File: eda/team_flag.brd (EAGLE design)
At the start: 40.6 x 40.6 mm, 25 parts, among them Q1 IRFML8244, Q2 IRFML8244

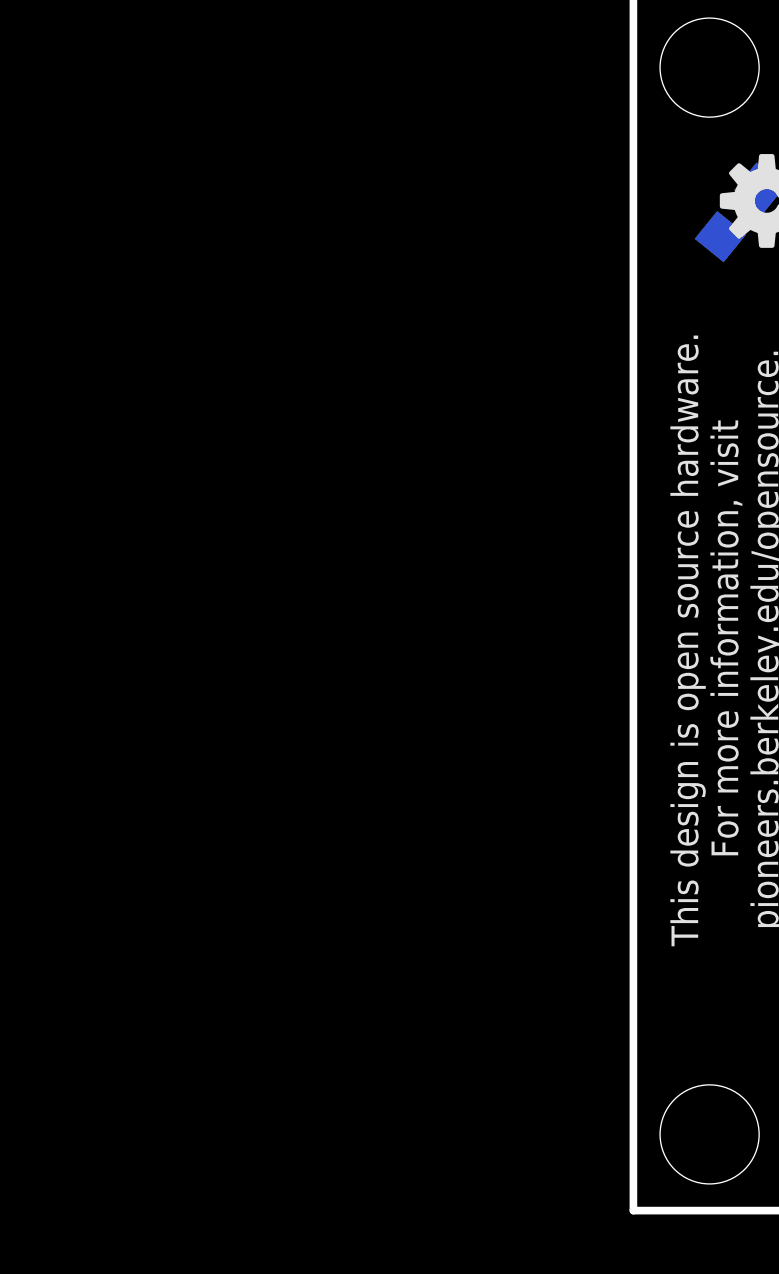
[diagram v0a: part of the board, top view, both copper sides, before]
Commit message: Add Arduino Pro Micro breakout and connect nets on schematic
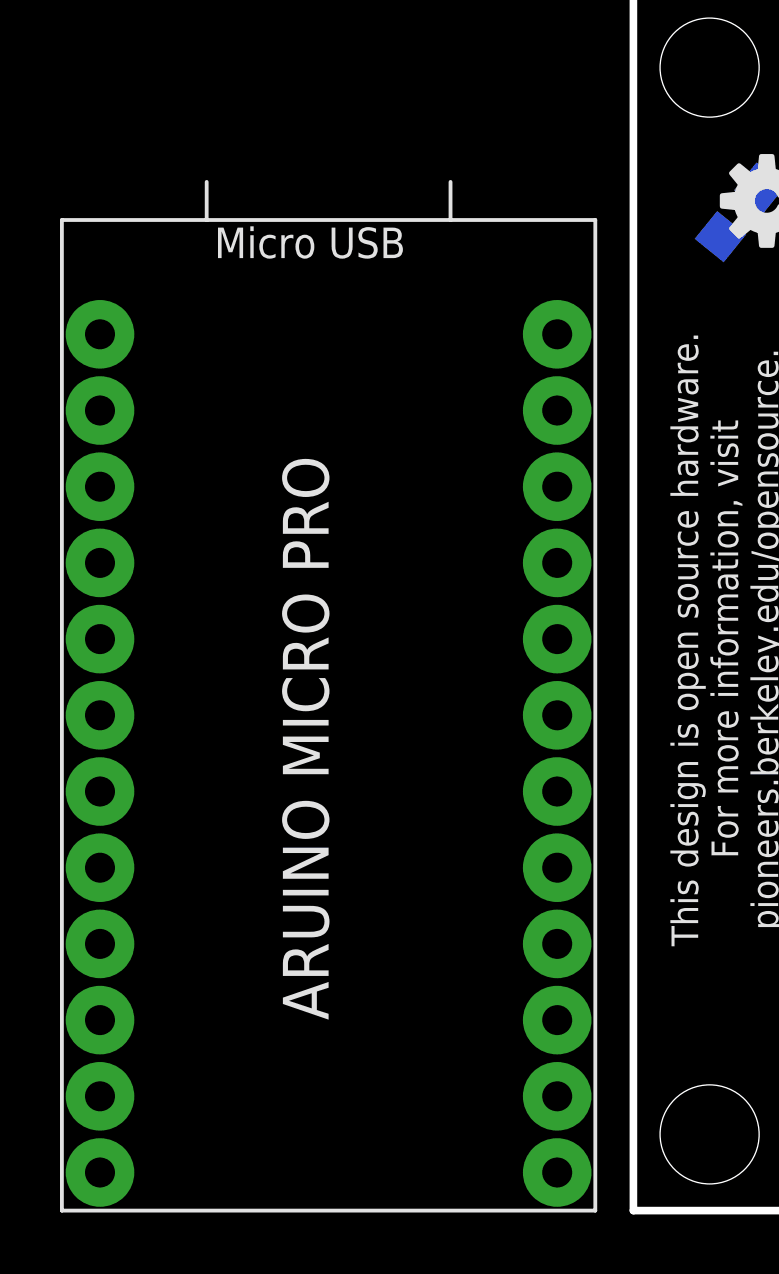
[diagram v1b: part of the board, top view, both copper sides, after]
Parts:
- added U$3: ARDUINO_PRO_MICRO, pie:ARDUINO_PRO_MICRO
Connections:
- net 5V: now also U$3.VCC
- net BLUE(IO1): now also U$3.5
- net GND: now also U$3.GND@0, U$3.GND@1, U$3.GND@2
- net LED1: now also U$3.A3
- net LED2: now also U$3.A2
- net LED3: now also U$3.A1
- net LED4: now also U$3.A0
- net YELLOW(IO2): now also U$3.6
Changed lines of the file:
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@@
 <layer number="54" name="bGND_GNDA" color="1" fill="9" visible="no" active="no"/>
 <layer number="56" name="wert" color="7" fill="1" visible="no" active="no"/>
+<layer number="57" name="tCAD" color="7" fill="1" visible="no" active="no"/>
+<layer number="59" name="tCarbon" color="7" fill="1" visible="no" active="no"/>
+<layer number="60" name="bCarbon" color="7" fill="1" visible="no" active="no"/>
 <layer number="90" name="Modules" color="5" fill="1" visible="no" active="no"/>
 <layer number="91" name="Nets" color="2" fill="1" visible="no" active="no"/>
@@
 <layer number="109" name="fp9" color="7" fill="1" visible="yes" active="yes"/>
 <layer number="110" name="fp0" color="7" fill="1" visible="yes" active="yes"/>
+<layer number="111" name="LPC17xx" color="7" fill="1" visible="yes" active="yes"/>
+<layer number="112" name="tSilk" color="7" fill="1" visible="yes" active="yes"/>
+<layer number="113" name="IDFDebug" color="7" fill="1" visible="yes" active="yes"/>
+<layer number="114" name="Badge_Outline" color="11" fill="1" visible="no" active="no"/>
 <layer number="116" name="Patch_BOT" color="9" fill="4" visible="yes" active="yes"/>
+<layer number="118" name="Rect_Pads" color="7" fill="1" visible="yes" active="yes"/>
 <layer number="121" name="_tsilk" color="7" fill="1" visible="yes" active="yes"/>
 <layer number="122" name="_bsilk" color="7" fill="1" visible="yes" active="yes"/>
@@
 <layer number="124" name="bTestmark" color="7" fill="1" visible="yes" active="yes"/>
 <layer number="125" name="_tNames" color="7" fill="1" visible="yes" active="yes"/>
+<layer number="126" name="_bNames" color="7" fill="1" visible="yes" active="yes"/>
+<layer number="127" name="_tValues" color="7" fill="1" visible="yes" active="yes"/>
+<layer number="128" name="_bValues" color="7" fill="1" visible="yes" active="yes"/>
+<layer number="129" name="Mask" color="7" fill="1" visible="yes" active="yes"/>
 <layer number="131" name="tAdjust" color="7" fill="1" visible="yes" active="yes"/>
 <layer number="132" name="bAdjust" color="7" fill="1" visible="yes" active="yes"/>
 <layer number="144" name="Drill_legend" color="7" fill="1" visible="yes" active="yes"/>
+<layer number="150" name="Notes" color="7" fill="1" visible="yes" active="yes"/>
 <layer number="151" name="HeatSink" color="7" fill="1" visible="yes" active="yes"/>
+<layer number="152" name="_bDocu" color="7" fill="1" visible="yes" active="yes"/>
+<layer number="153" name="FabDoc1" color="7" fill="1" visible="yes" active="yes"/>
+<layer number="154" name="FabDoc2" color="7" fill="1" visible="yes" active="yes"/>
+<layer number="155" name="FabDoc3" color="7" fill="1" visible="yes" active="yes"/>
 <layer number="199" name="Contour" color="7" fill="1" visible="yes" active="yes"/>
 <layer number="200" name="200bmp" color="1" fill="10" visible="yes" active="yes"/>
@@
 <layer number="223" name="223bmp" color="24" fill="1" visible="no" active="no"/>
 <layer number="224" name="224bmp" color="25" fill="1" visible="no" active="no"/>
+<layer number="225" name="225bmp" color="7" fill="1" visible="yes" active="yes"/>
+<layer number="226" name="226bmp" color="7" fill="1" visible="yes" active="yes"/>
+<layer number="227" name="227bmp" color="7" fill="1" visible="yes" active="yes"/>
+<layer number="228" name="228bmp" color="7" fill="1" visible="yes" active="yes"/>
+<layer number="229" name="229bmp" color="7" fill="1" visible="yes" active="yes"/>
+<layer number="230" name="230bmp" color="7" fill="1" visible="yes" active="yes"/>
+<layer number="231" name="231bmp" color="7" fill="1" visible="yes" active="yes"/>
+<layer number="248" name="Housing" color="7" fill="1" visible="yes" active="yes"/>
+<layer number="249" name="Edge" color="7" fill="1" visible="yes" active="yes"/>
 <layer number="250" name="Descript" color="3" fill="1" visible="no" active="no"/>
 <layer number="251" name="SMDround" color="12" fill="11" visible="no" active="no"/>
 <layer number="254" name="cooling" color="7" fill="1" visible="yes" active="yes"/>
+<layer number="255" name="routoute" color="7" fill="1" visible="yes" active="yes"/>
 </layers>
 <board>
@@
 <attribute name="VALUE" x="5.45880625" y="31.758984375" size="0.762" layer="26" font="vector" ratio="15" rot="MR309" align="center"/>
 </element>
+<element name="U$3" library="pie" package="ARDUINO_PRO_MICRO" value="ARDUINO_PRO_MICRO" x="-19.05" y="0"/>
 </elements>
 <signals>
@@
 <wire x1="17.46" y1="13.777" x2="17.78" y2="14.097" width="0.3048" layer="1"/>
 <wire x1="17.78" y1="14.097" x2="19.431" y2="14.097" width="0.3048" layer="1"/>
+<contactref element="U$3" pad="6"/>
+<wire x1="-17.78" y1="8.89" x2="17.46" y2="12.938" width="0" layer="19" extent="1-1"/>
 </signal>
 <signal name="GND">
@@
 <via x="13.97" y="26.67" extent="1-16" drill="0.5"/>
 <via x="15.24" y="27.94" extent="1-16" drill="0.5"/>
+<contactref element="U$3" pad="GND@1"/>
+<contactref element="U$3" pad="GND@0"/>
+<contactref element="U$3" pad="GND@2"/>
+<wire x1="32.46468125" y1="37.739371875" x2="36.428628125" y2="34.08331875" width="0" layer="19" extent="16-16"/>
+<wire x1="15.24" y1="27.94" x2="32.46468125" y2="37.739371875" width="0" layer="19" extent="16-16"/>
+<wire x1="13.97" y1="27.94" x2="15.24" y2="27.94" width="0" layer="19" extent="1-1"/>
+<wire x1="12.7" y1="27.94" x2="13.97" y2="27.94" width="0" layer="19" extent="1-1"/>
+<wire x1="13.97" y1="26.67" x2="13.97" y2="27.94" width="0" layer="19" extent="1-1"/>
+<wire x1="6.55668125" y1="36.555625" x2="13.97" y2="30.48" width="0" layer="19" extent="1-16"/>
+<wire x1="2.900628125" y1="32.464678125" x2="6.55668125" y2="36.555625" width="0" layer="19" extent="16-16"/>
+<wire x1="-2.54" y1="26.67" x2="2.900628125" y2="32.464678125" width="0" layer="19" extent="16-16"/>
+<wire x1="15.24" y1="15.025" x2="13.97" y2="26.67" width="0" layer="19" extent="1-1"/>
+<wire x1="15.56" y1="12.938" x2="15.24" y2="15.025" width="0" layer="19" extent="1-1"/>
+<wire x1="20.64" y1="12.938" x2="15.56" y2="12.938" width="0" layer="19" extent="1-1"/>
+<wire x1="20.3454" y1="16.725" x2="20.64" y2="12.938" width="0" layer="19" extent="1-1"/>
+<wire x1="25.4254" y1="16.725" x2="20.3454" y2="16.725" width="0" layer="19" extent="1-1"/>
+<wire x1="-17.78" y1="24.13" x2="-2.54" y2="26.67" width="0" layer="19" extent="1-1"/>
+<wire x1="-17.78" y1="21.59" x2="-17.78" y2="24.13" width="0" layer="19" extent="1-1"/>
 </signal>
 <signal name="BLUE(IO1)">
@@
 <wire x1="22.54" y1="13.777" x2="22.86" y2="14.097" width="0.3048" layer="1"/>
 <wire x1="22.86" y1="14.097" x2="24.511" y2="14.097" width="0.3048" layer="1"/>
+<contactref element="U$3" pad="5"/>
+<wire x1="-17.78" y1="11.43" x2="21.59" y2="7.62" width="0" layer="19" extent="1-1"/>
 </signal>
 <signal name="BSOURCE">
@@
 <wire x1="26.67" y1="25.4" x2="26.67" y2="21.59" width="0.762" layer="1"/>
 <wire x1="26.67" y1="21.59" x2="25.4" y2="20.32" width="0.762" layer="1"/>
+<contactref element="U$3" pad="VCC"/>
+<wire x1="-2.54" y1="21.59" x2="15.24" y2="20.32" width="0" layer="19" extent="16-16"/>
 </signal>
 <signal name="LED4">
@@
 <wire x1="12.7" y1="25.4" x2="16.51" y2="25.4" width="0.3048" layer="1"/>
 <wire x1="11.43" y1="26.67" x2="12.7" y2="25.4" width="0.3048" layer="1"/>
+<contactref element="U$3" pad="A0"/>
+<wire x1="-2.54" y1="11.43" x2="12.7" y2="25.4" width="0" layer="19" extent="1-1"/>
 </signal>
 <signal name="N$4">
@@
 <wire x1="26.67" y1="30.9" x2="24.55" y2="30.9" width="0.3048" layer="1"/>
 <wire x1="24.55" y1="30.9" x2="24.13" y2="30.48" width="0.3048" layer="1"/>
+<contactref element="U$3" pad="A3"/>
+<wire x1="-2.54" y1="19.05" x2="24.13" y2="30.48" width="0" layer="19" extent="1-1"/>
 </signal>
 <signal name="LED2">
@@
 <contactref element="JP1" pad="P$3"/>
 <wire x1="21.59" y1="30.9" x2="21.59" y2="25.4" width="0.3048" layer="1"/>
+<contactref element="U$3" pad="A2"/>
+<wire x1="-2.54" y1="16.51" x2="21.59" y2="25.4" width="0" layer="19" extent="1-1"/>
 </signal>
 <signal name="LED3">
@@
 <wire x1="16.51" y1="30.9" x2="18.63" y2="30.9" width="0.3048" layer="1"/>
 <wire x1="18.63" y1="30.9" x2="19.05" y2="30.48" width="0.3048" layer="1"/>
+<contactref element="U$3" pad="A1"/>
+<wire x1="-2.54" y1="13.97" x2="16.51" y2="30.9" width="0" layer="19" extent="1-1"/>
 </signal>
 </signals>

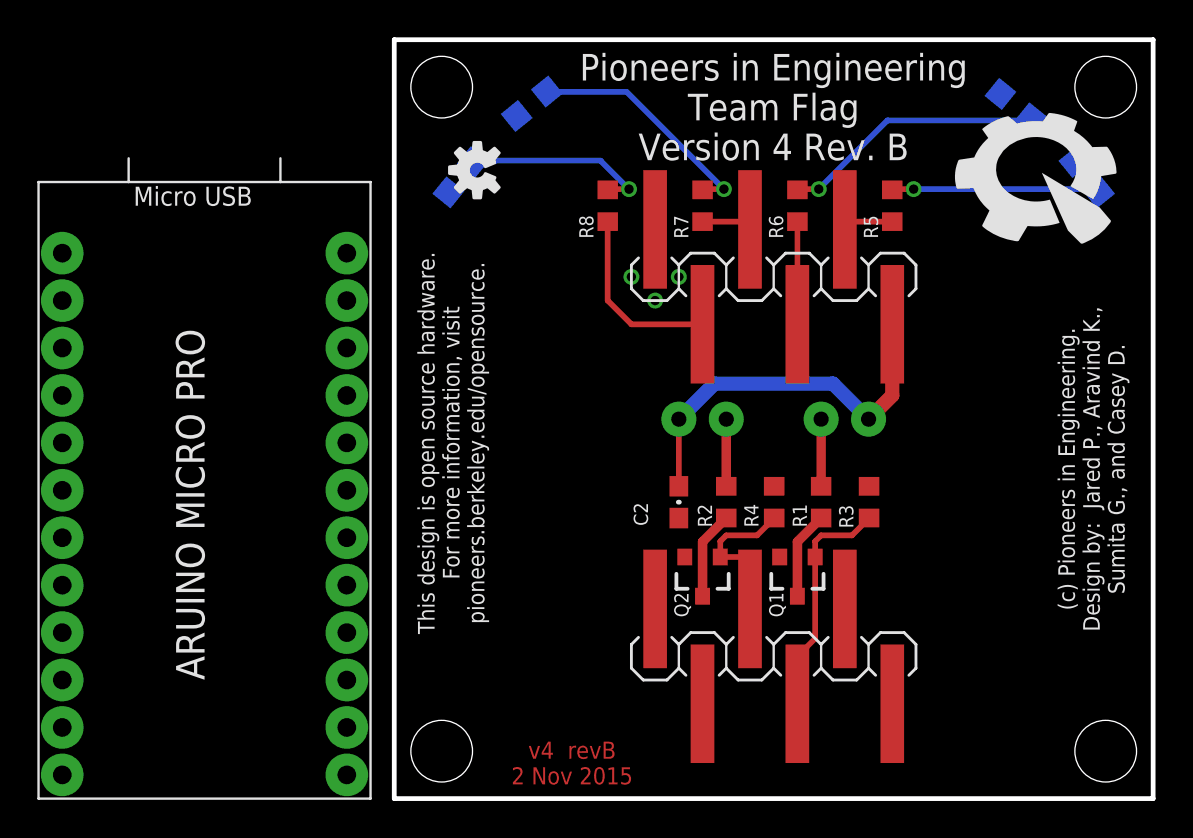
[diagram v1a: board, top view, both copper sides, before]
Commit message: Finished routing team flag board (now with Arduino ProMicro)
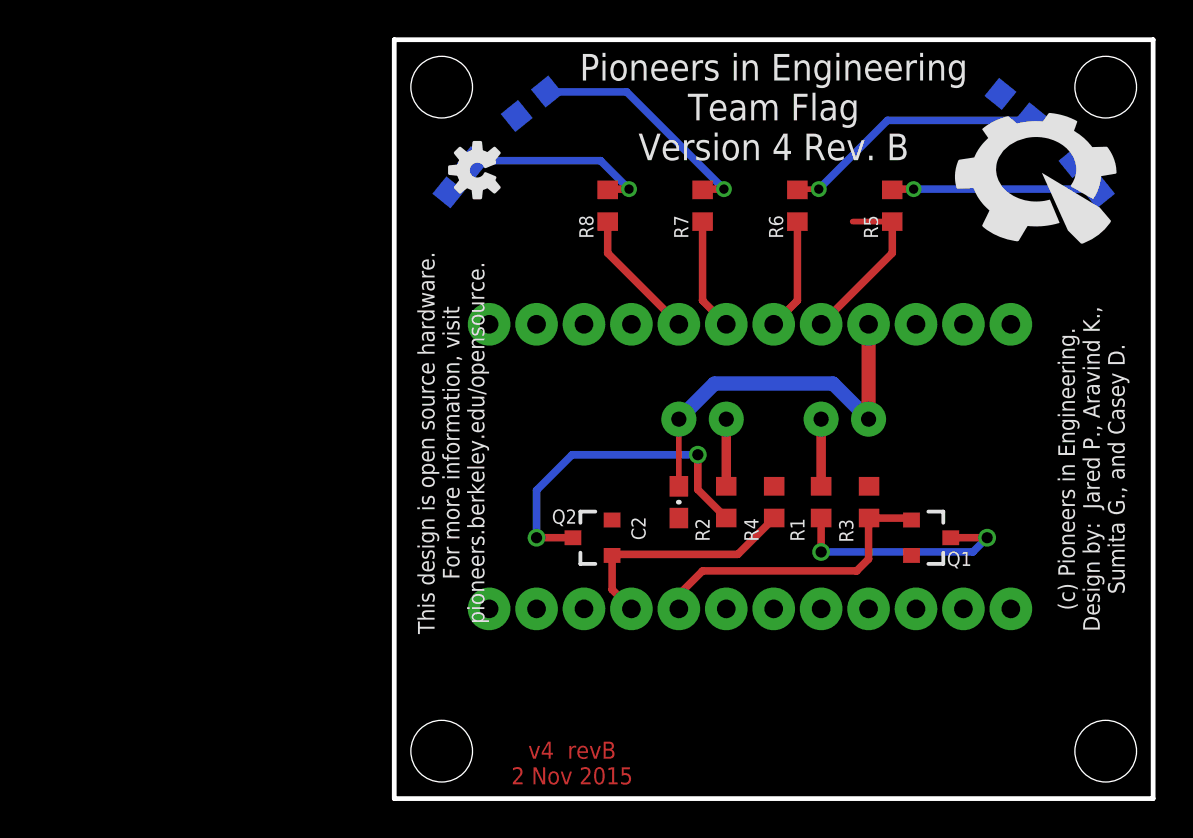
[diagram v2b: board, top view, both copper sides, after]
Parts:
- removed JP1, JP2: (no value), pie:1X06-SMD-C
- moved U$3 24.5 mm to (3.81, 8.89), flipped to the bottom, turned to 90 degrees
- moved Q1 7.40 mm to (28.7, 14.0), turned to 270 degrees
- moved Q2 6.19 mm to (10.7, 14.0), turned to 90 degrees
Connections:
- net N$1 renamed LED2R
- net N$4 renamed LED1R
- net N$5 renamed LED3R
- net N$6 renamed LED4R
- net 5V: no longer JP1.P$1
- net BLUE(IO1): no longer JP2.P$3
- net GND: no longer JP1.P$6
- net LED1: no longer JP1.P$2
- net LED2: no longer JP1.P$3
- net LED3: no longer JP1.P$4
- net LED4: no longer JP1.P$5
- net YELLOW(IO2): no longer JP2.P$4
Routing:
- net YSOURCE: track 4.71 -> 17.9 mm, vias 0 -> 2
- net BSOURCE: track 4.71 -> 13.0 mm, vias 0 -> 2
- net LED1: track 2.71 -> 9.20 mm
- net YELLOW(IO2): track 8.64 -> 12.8 mm
- net BLUE(IO1): track 12.5 -> 16.2 mm
- net LED3: track 2.71 -> 6.03 mm
- net LED4: track 9.84 -> 7.08 mm
- net GND: track 2.54 -> 0.00 mm, vias 3 -> 0
- net 5V: track 20.9 -> 20.4 mm
- net LED2: track 5.50 -> 6.03 mm
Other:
- board text removed: "Smart Device"

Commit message: Update revision info for Team Flag
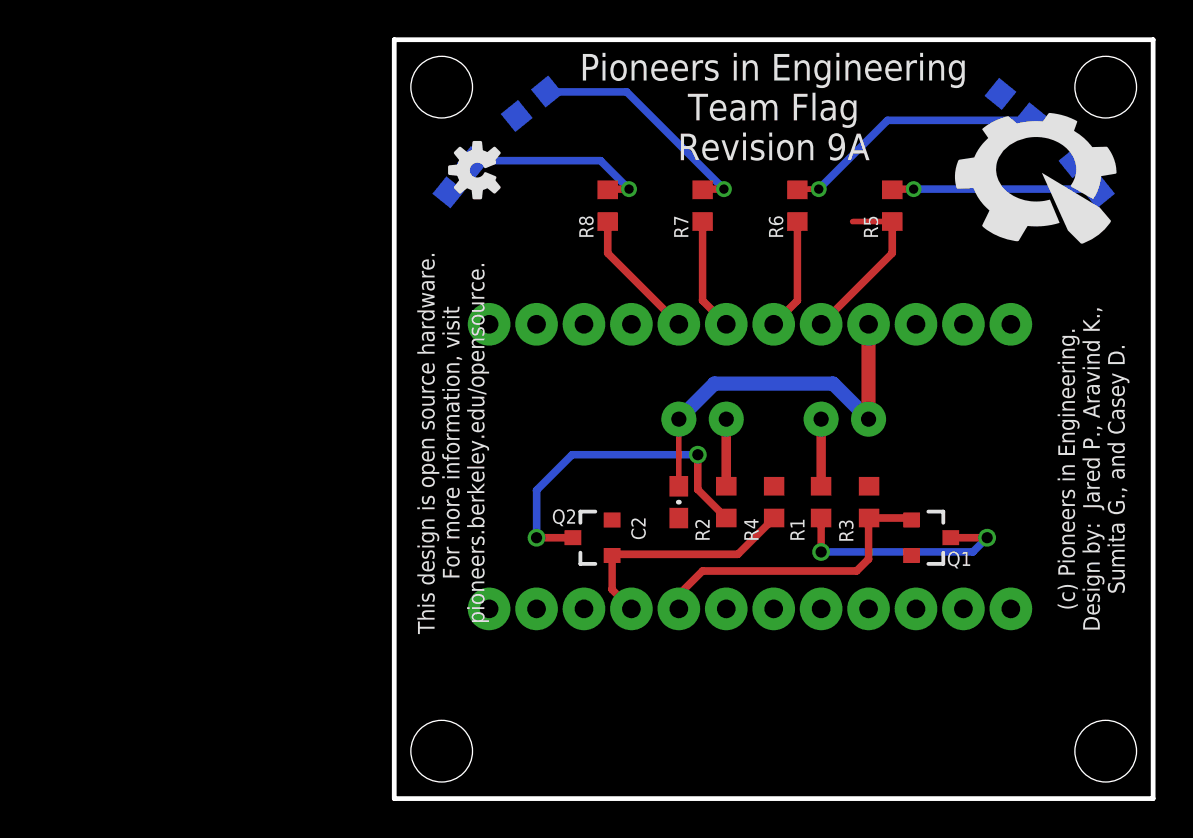
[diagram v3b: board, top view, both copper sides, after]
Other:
- board text added: "Pioneers in Engineering Team Flag Revision 9A"
- board text removed: "Pioneers in Engineering Team Flag Version 4 Rev. B"
- board text removed: "v4 revB 2 Nov 2015"
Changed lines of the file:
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@@
 <layer number="14" name="Route14" color="1" fill="6" visible="no" active="no"/>
 <layer number="15" name="Route15" color="4" fill="6" visible="no" active="no"/>
-<layer number="16" name="Bottom" color="1" fill="1" visible="yes" active="yes"/>
+<layer number="16" name="Bottom" color="1" fill="1" visible="no" active="yes"/>
 <layer number="17" name="Pads" color="2" fill="1" visible="yes" active="yes"/>
 <layer number="18" name="Vias" color="2" fill="1" visible="yes" active="yes"/>
@@
 <layer number="20" name="Dimension" color="15" fill="1" visible="yes" active="yes"/>
 <layer number="21" name="tPlace" color="16" fill="1" visible="yes" active="yes"/>
-<layer number="22" name="bPlace" color="17" fill="1" visible="yes" active="yes"/>
+<layer number="22" name="bPlace" color="17" fill="1" visible="no" active="yes"/>
 <layer number="23" name="tOrigins" color="15" fill="1" visible="yes" active="yes"/>
-<layer number="24" name="bOrigins" color="15" fill="1" visible="yes" active="yes"/>
+<layer number="24" name="bOrigins" color="15" fill="1" visible="no" active="yes"/>
 <layer number="25" name="tNames" color="18" fill="1" visible="yes" active="yes"/>
-<layer number="26" name="bNames" color="19" fill="1" visible="yes" active="yes"/>
+<layer number="26" name="bNames" color="19" fill="1" visible="no" active="yes"/>
 <layer number="27" name="tValues" color="18" fill="1" visible="yes" active="yes"/>
-<layer number="28" name="bValues" color="19" fill="1" visible="yes" active="yes"/>
+<layer number="28" name="bValues" color="19" fill="1" visible="no" active="yes"/>
 <layer number="29" name="tStop" color="7" fill="3" visible="yes" active="yes"/>
 <layer number="30" name="bStop" color="7" fill="6" visible="yes" active="yes"/>
@@
 <text x="20.32" y="39.878" size="1.4224" layer="21" font="vector" ratio="15" rot="R180" align="bottom-center">Pioneers in Engineering
 Team Flag
-Version 4 Rev. B</text>
+Revision 9A</text>
 <text x="35.56" y="17.653" size="0.889" layer="21" font="vector" ratio="15" rot="R270" align="bottom-center">(c) Pioneers in Engineering.
 Design by:  Jared P., Aravind K.,
 Sumita G., and Casey D.</text>
-<text x="9.525" y="3.048" size="0.9144" layer="1" font="vector" ratio="20" rot="R180" align="bottom-center">v4  revB
-2 Nov 2015</text>
 <text x="1.27" y="19.05" size="0.889" layer="21" font="vector" ratio="15" rot="R270" align="bottom-center">This design is open source hardware.
 For more information, visit
